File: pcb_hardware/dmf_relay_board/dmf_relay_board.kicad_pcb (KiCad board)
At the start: 4 copper layers, 100 x 96.5 mm, 76 parts, among them J1 HVPS, J2 Relays to Electrodes 1, J3 Relays to Electrodes 2, J4 Electrodes from Relay 1, J5 Electrodes from Relay 2, M1 MountingHole_3.2mm_M3, M2 MountingHole_3.2mm_M3, M3 MountingHole_3.2mm_M3, M4 MountingHole_3.2mm_M3, M5 MountingHole_3.2mm_M3, M6 MountingHole_3.2mm_M3, U1 HV507

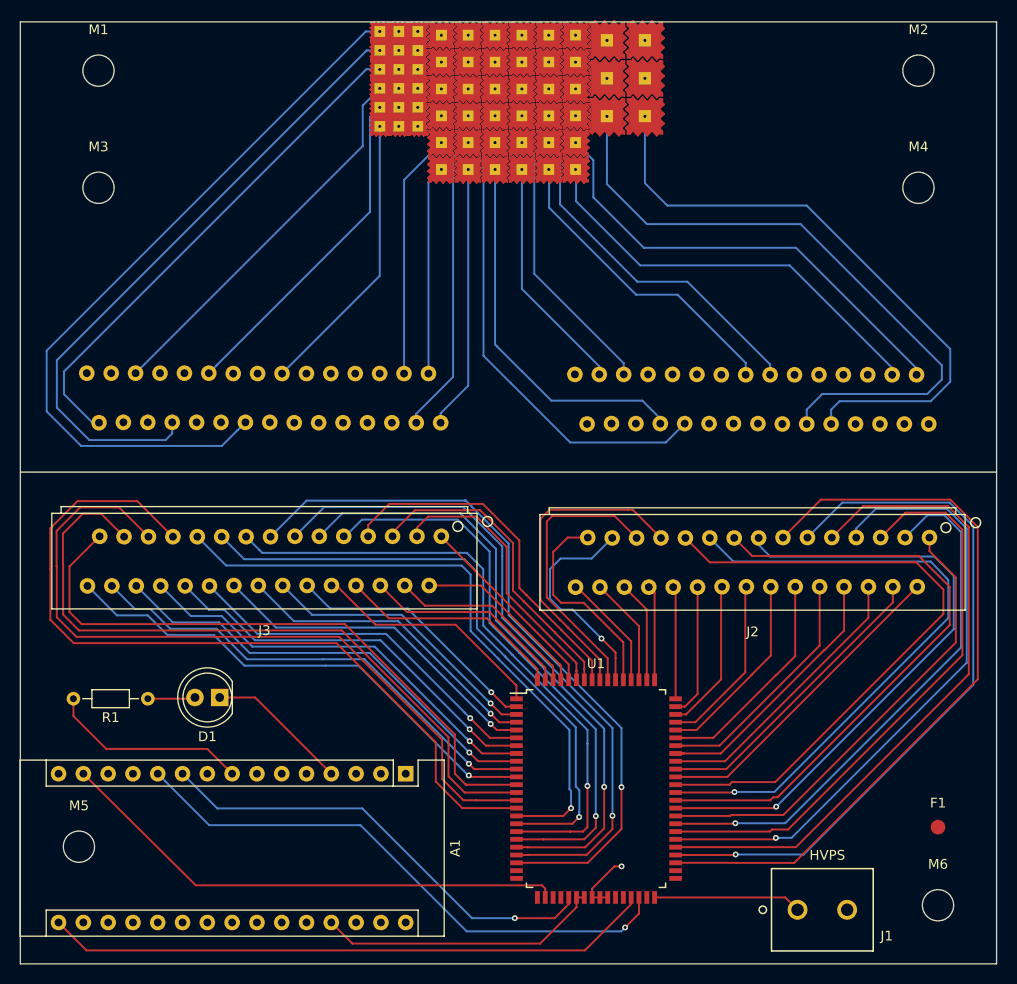
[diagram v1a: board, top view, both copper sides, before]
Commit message: hvps and low voltage isolated
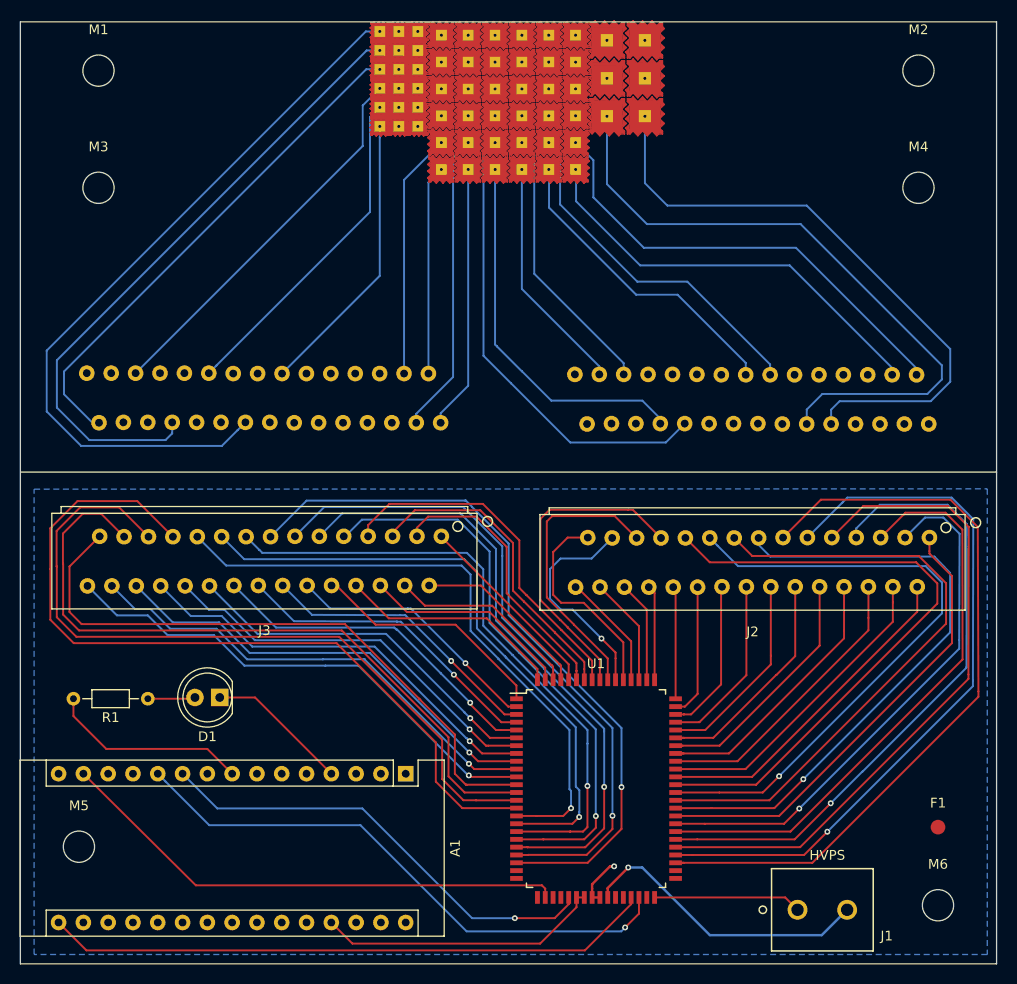
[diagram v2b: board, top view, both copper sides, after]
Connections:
- J1 pad 2: GND -> GNDPWR
- U1 pad 34: GND -> GNDPWR
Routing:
- net GNDPWR: track 0.00 -> 30.3 mm, vias 0 -> 1
- net CHNL_3: track 77.1 -> 79.0 mm
- net CHNL_12: track 65.5 -> 63.7 mm
- net CHNL_14: track 32.8 -> 34.3 mm
- net CHNL_13: track 65.8 -> 64.3 mm
- net GND: track 21.1 -> 19.8 mm
- net CHNL_15: track 30.9 -> 32.1 mm
- net CHNL_4: track 73.5 -> 74.3 mm
- net CHNL_6: track 65.0 -> 65.9 mm
- net CHNL_16: track 29.0 -> 29.8 mm
- net CHNL_11: track 63.6 -> 63.0 mm
- net CHNL_8: track 56.0 -> 55.4 mm
- net CHNL_9: track 47.9 -> 47.4 mm
- net CHNL_20: track 20.0 -> 20.5 mm
- added copper zone on B.Cu, net GND
- removed copper zone on In2.Cu, net GND
- removed copper zone on In1.Cu, net VPP
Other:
- net class DMF_HV: clearance 0.2 -> 0.4

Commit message: hv power isolated
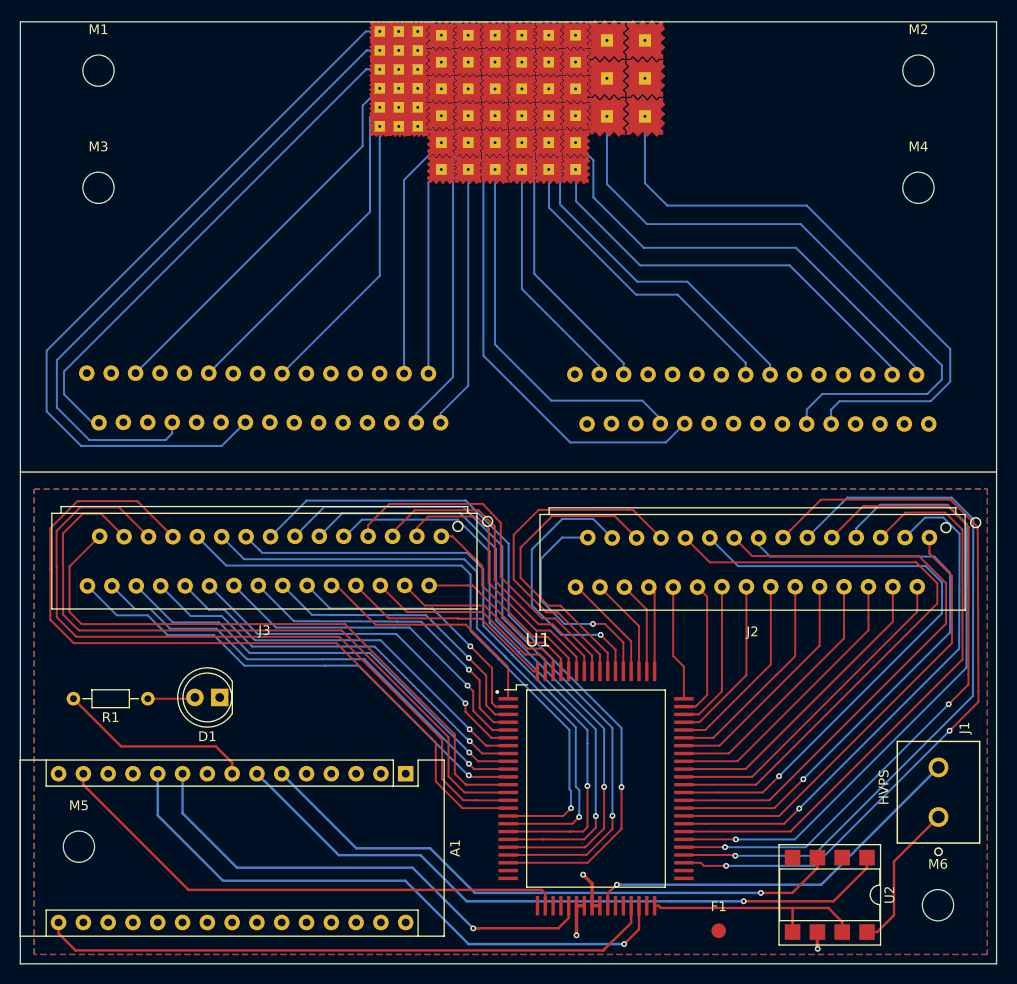
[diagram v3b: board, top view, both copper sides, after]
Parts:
- added U2: AQW210EHAX, Package_DIP:DIP-8_W7.62mm_SMDSocket_SmallPads, F.Cu at (194.9, 143.5)
- U1: footprint Package_QFP:PQFP-80_14x20mm_P0.8mm -> HV507:QFP80P2390X1790X340-80N
- moved F1 24.8 mm to (183.5, 147.2)
- moved J1 17.3 mm to (206.0, 135.5), turned to 90 degrees
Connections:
- A1 pad 6: Net-(A1-Pad6) -> RELAY_VDD
- A1 pad 7: Net-(A1-Pad7) -> RELAY_VPP
- J1 pad 1: VPP -> HVPS_VPP
- U1 pad 40: VPP -> HV507_VPP
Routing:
- net RELAY_VPP: track 0.00 -> 70.4 mm, vias 0 -> 1
- net RELAY_VDD: track 0.00 -> 62.0 mm, vias 0 -> 1
- net HV507_VPP: track 0.00 -> 23.4 mm
- net VDD: track 29.4 -> 6.56 mm, vias 0 -> 2
- net GND: track 19.8 -> 4.37 mm
- net HVPS_VPP: track 0.00 -> 15.4 mm
- net VPP: track 15.2 -> 0.00 mm
- net GNDPWR: track 30.3 -> 40.5 mm
- net CHNL_30: track 22.5 -> 28.7 mm
- net ~LE: track 58.4 -> 63.8 mm
- net CHNL_32: track 32.9 -> 37.2 mm
- net ~BL: track 47.0 -> 50.9 mm
- net CHNL_29: track 21.6 -> 24.0 mm, vias 0 -> 1
- net CHNL_44: track 32.2 -> 34.6 mm
- net CHNL_36: track 20.1 -> 22.4 mm
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- added copper zone on F.Cu, net GND
- added copper zone on B.Cu, net VDD
- removed copper zone on B.Cu, net GND

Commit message: minor changes
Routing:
- net GND: track 4.37 -> 3.81 mm
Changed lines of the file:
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@@
   (gr_line (start 111.9735 54.0412) (end 111.9735 150.536) (layer Edge.Cuts) (width 0.05))
   (gr_line (start 111.9735 150.536) (end 211.9735 150.536) (layer Edge.Cuts) (width 0.05))
-  (via (at 169.6212 141.4018) (size 0.6) (drill 0.3) (layers F.Cu B.Cu) (net 7))
-  (segment (start 170.542 142.3226) (end 169.6212 141.4018) (width 0.35) (layer F.Cu) (net 7))
-  (segment (start 170.542 142.3226) (end 170.542 144.588) (width 0.35) (layer F.Cu) (net 7))
+  (via (at 169.70756 141.92504) (size 0.6) (drill 0.3) (layers F.Cu B.Cu) (net 7))
   (segment (start 170.542 144.588) (end 171.342 144.588) (width 0.35) (layer F.Cu) (net 7))
+  (segment (start 170.542 142.75948) (end 170.542 144.588) (width 0.35) (layer F.Cu) (net 7))
+  (segment (start 169.70756 141.92504) (end 170.542 142.75948) (width 0.35) (layer F.Cu) (net 7))
   (segment (start 133.6675 129.93263) (end 131.99979 128.26492) (width 0.25) (layer F.Cu) (net 13))
   (segment (start 133.6675 131.064) (end 133.6675 129.93263) (width 0.25) (layer F.Cu) (net 13))
@@
   (segment (start 179.942 140.188) (end 179.95184 140.19784) (width 0.2) (layer F.Cu) (net 67))
   (segment (start 179.092 140.188) (end 179.942 140.188) (width 0.2) (layer F.Cu) (net 67))
-  (via (at 207.1624 126.65964) (size 0.6) (drill 0.3) (layers F.Cu B.Cu) (net 67))
-  (segment (start 193.97608 102.99192) (end 190.0975 106.8705) (width 0.2) (layer F.Cu) (net 67))
-  (segment (start 210.04784 105.79354) (end 207.24622 102.99192) (width 0.2) (layer F.Cu) (net 67))
-  (segment (start 207.462399 126.359641) (end 207.467479 126.359641) (width 0.2) (layer F.Cu) (net 67))
-  (segment (start 207.1624 126.65964) (end 207.462399 126.359641) (width 0.2) (layer F.Cu) (net 67))
-  (segment (start 207.467479 126.359641) (end 210.11388 123.71324) (width 0.2) (layer F.Cu) (net 67))
-  (segment (start 207.24622 102.99192) (end 193.97608 102.99192) (width 0.2) (layer F.Cu) (net 67))
-  (segment (start 210.11388 123.71324) (end 210.11388 122.6312) (width 0.2) (layer F.Cu) (net 67))
-  (segment (start 210.11388 122.6312) (end 210.04784 105.79354) (width 0.2) (layer F.Cu) (net 67))
   (segment (start 179.942 140.188) (end 181.68144 140.188) (width 0.2) (layer F.Cu) (net 67))
   (via (at 184.277 140.49756) (size 0.6) (drill 0.3) (layers F.Cu B.Cu) (net 67))
@@
   (segment (start 184.277 140.49756) (end 193.32448 140.49756) (width 0.2) (layer B.Cu) (net 67))
   (segment (start 193.32448 140.49756) (end 193.6496 140.17244) (width 0.2) (layer B.Cu) (net 67))
+  (via (at 209.2706 124.5362) (size 0.6) (drill 0.3) (layers F.Cu B.Cu) (net 67))
+  (segment (start 207.1624 126.65964) (end 207.1624 126.6444) (width 0.2) (layer B.Cu) (net 67))
+  (segment (start 207.1624 126.6444) (end 209.2706 124.5362) (width 0.2) (layer B.Cu) (net 67))
+  (segment (start 193.97608 102.99192) (end 190.0975 106.8705) (width 0.2) (layer F.Cu) (net 67))
+  (segment (start 210.11388 123.69292) (end 210.11388 122.6312) (width 0.2) (layer F.Cu) (net 67))
+  (segment (start 209.2706 124.5362) (end 210.11388 123.69292) (width 0.2) (layer F.Cu) (net 67))
+  (segment (start 210.11388 122.6312) (end 210.04784 105.79354) (width 0.2) (layer F.Cu) (net 67))
+  (segment (start 210.04784 105.79354) (end 207.24622 102.99192) (width 0.2) (layer F.Cu) (net 67))
+  (segment (start 207.24622 102.99192) (end 193.97608 102.99192) (width 0.2) (layer F.Cu) (net 67))
   (segment (start 179.092 139.388) (end 180.82556 139.388) (width 0.2) (layer F.Cu) (net 68))
   (segment (start 179.942 139.388) (end 185.12324 139.388) (width 0.2) (layer F.Cu) (net 68))

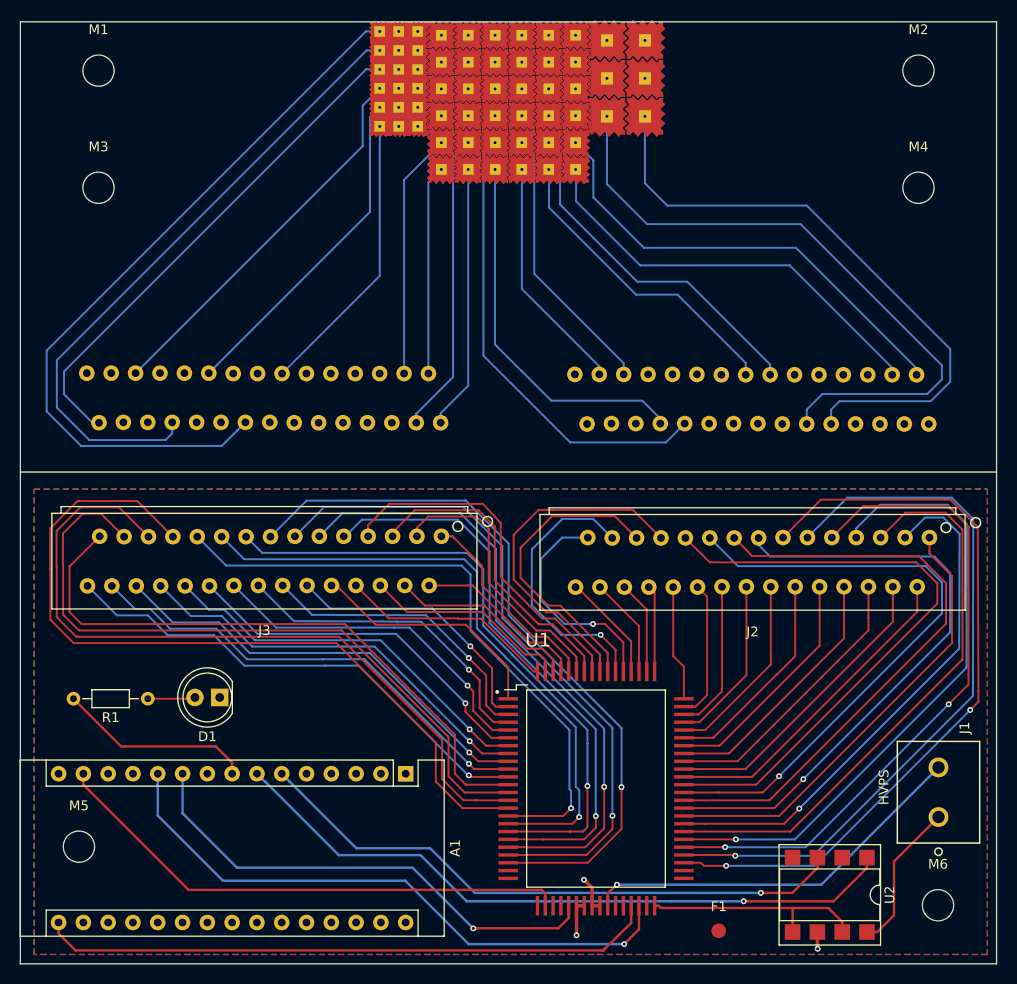
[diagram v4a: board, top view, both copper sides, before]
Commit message: pull-resistors for relays
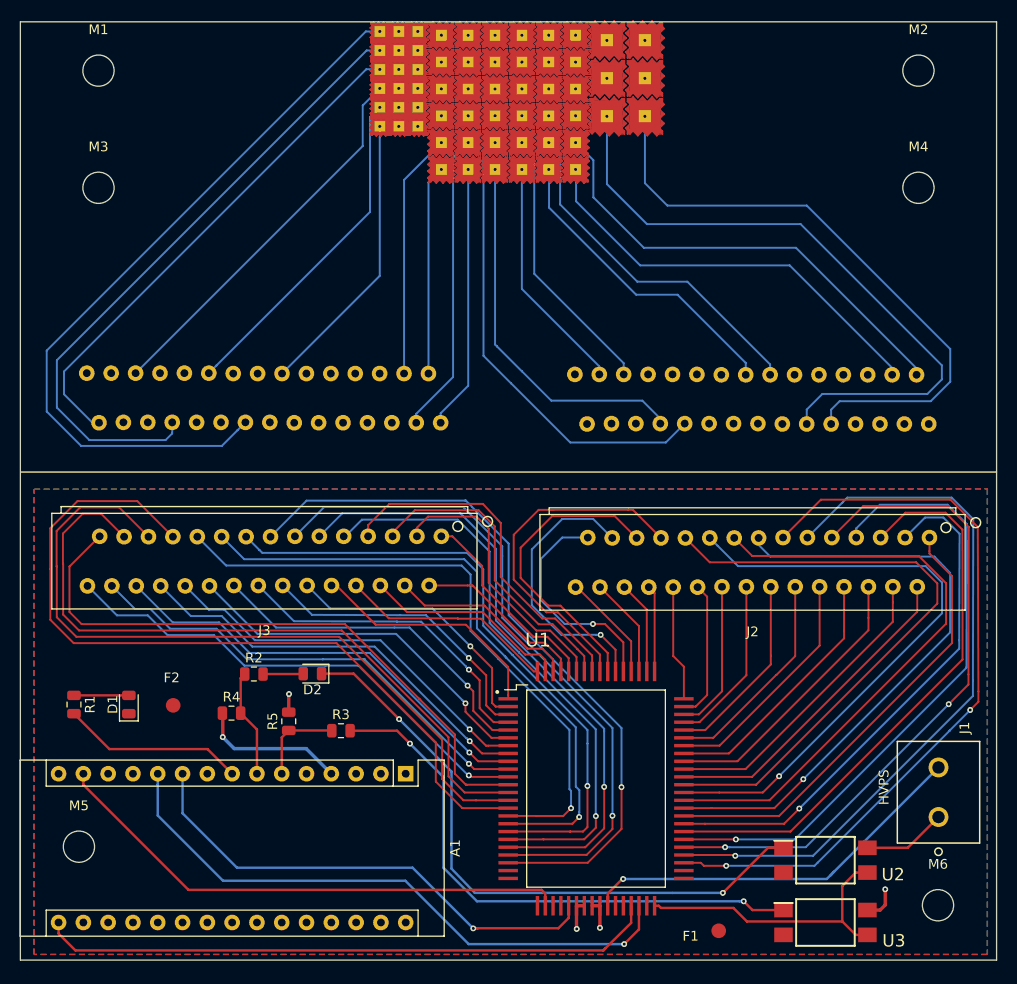
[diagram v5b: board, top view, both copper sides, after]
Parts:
- added D2: GREEN LED, LED_SMD:LED_0805_2012Metric, F.Cu at (141.9, 120.8)
- added F2: Fiducial_1.5mm_Mask3mm, Fiducial:Fiducial_1.5mm_Mask3mm, F.Cu at (127.6, 124.1)
- added R2: 750, Resistor_SMD:R_0805_2012Metric, F.Cu at (135.9, 120.9)
- added R3: 560, Resistor_SMD:R_0805_2012Metric, F.Cu at (144.8, 126.7)
- added R4: 10k, Resistor_SMD:R_0805_2012Metric, F.Cu at (133.6, 124.9)
- added R5: 330, Resistor_SMD:R_0805_2012Metric, F.Cu at (139.5, 125.7)
- added U3: AQY210EHA, SamacSys_Parts:SOP254P962X315-4N, F.Cu at (194.4, 146.3)
- D1: value LED -> BLUE LED; footprint LED_THT:LED_D5.0mm_FlatTop -> LED_SMD:LED_0805_2012Metric
- R1: value R -> 1k; footprint Resistor_THT:R_Axial_DIN0204_L3.6mm_D1.6mm_P7.62mm_Horizontal -> Resistor_SMD:R_0805_2012Metric
- U2: value AQW210EHAX -> AQY210EHA; footprint Package_DIP:DIP-8_W7.62mm_SMDSocket_SmallPads -> SamacSys_Parts:SOP254P962X315-4N
- moved D1 9.34 mm to (123.1, 124.0), turned to 90 degrees
- moved R1 7.59 mm to (117.5, 124.0), turned to 270 degrees
- moved U2 3.58 mm to (194.4, 139.9), turned to 0 degrees
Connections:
- A1 pad 6: RELAY_VDD -> Net-(A1-Pad6)
- A1 pad 7: RELAY_VPP -> Net-(A1-Pad7)
- U2 pad 1: RELAY_VPP -> VPP_ON
- U2 pad 3: RELAY_VDD -> HV507_VPP
- U2 pad 4: GND -> HVPS_VPP
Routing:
- net RELAY_VPP: track 70.4 -> 0.00 mm, vias 1 -> 0
- net VPP_ON: track 0.00 -> 64.4 mm, vias 0 -> 2
- net RELAY_VDD: track 62.0 -> 0.00 mm, vias 1 -> 0
- net VDD_ON: track 0.00 -> 57.4 mm, vias 0 -> 2
- net GND: track 3.81 -> 18.2 mm, vias 1 -> 2
- net Net-(A1-Pad7): track 0.00 -> 11.1 mm
- net Net-(A1-Pad6): track 0.00 -> 9.15 mm
- net HVPS_VPP: track 15.4 -> 8.59 mm
- net HV507_VPP: track 23.4 -> 29.8 mm
- net Net-(D2-Pad2): track 0.00 -> 4.76 mm
- net VDD: track 6.56 -> 9.70 mm, vias 2 -> 3
- net Net-(A1-Pad8): track 20.1 -> 18.8 mm
- net Net-(D1-Pad2): track 4.88 -> 5.62 mm
- net GNDPWR: track 40.5 -> 41.0 mm
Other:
- board size 100 x 96.5 mm -> 100 x 96.1 mm

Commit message: hv data direction fix
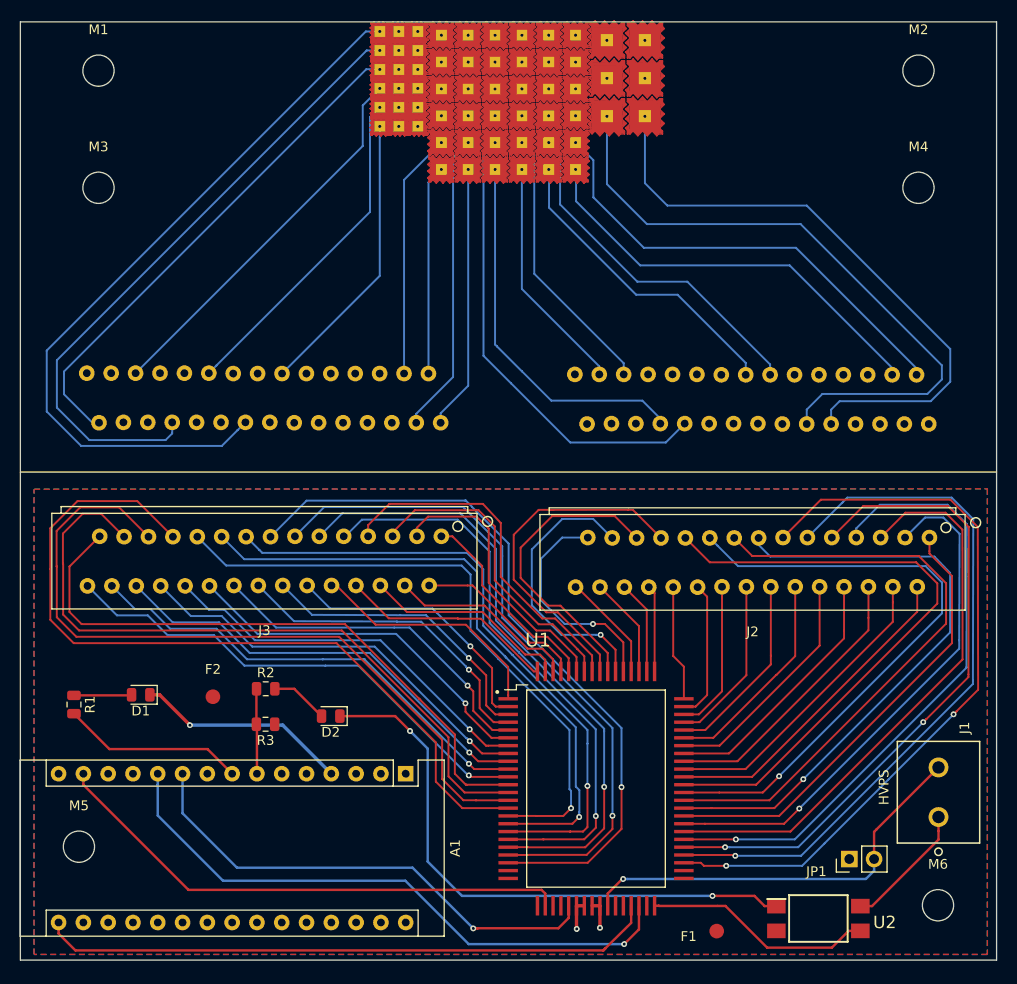
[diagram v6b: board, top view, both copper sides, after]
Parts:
- removed R4: 10k, Resistor_SMD:R_0805_2012Metric
- removed R5: 330, Resistor_SMD:R_0805_2012Metric
- removed U3: AQY210EHA, SamacSys_Parts:SOP254P962X315-4N
- added JP1: GND to HV-GND Jumper, Connector_PinHeader_2.54mm:PinHeader_1x02_P2.54mm_Vertical, F.Cu at (196.9, 139.8)
- R3: value 560 -> 10k
- moved R3 7.75 mm to (137.1, 126.0), turned to 180 degrees
- moved U2 6.02 mm to (193.7, 145.9)
- moved D2 4.74 mm to (143.8, 125.2)
- moved F2 4.17 mm to (131.7, 123.2)
- moved R2 1.94 mm to (137.1, 122.4)
- moved D1 1.57 mm to (124.3, 123.0), turned to 180 degrees
- moved F1 0.21 mm to (183.3, 147.2)
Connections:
- R3 pad 1: Net-(A1-Pad6) -> GND
- R3 pad 2: VDD_ON -> Net-(A1-Pad7)
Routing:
- net VDD_ON: track 57.4 -> 0.00 mm, vias 2 -> 0
- net Net-(A1-Pad6): track 9.15 -> 0.00 mm
- net GND: track 18.2 -> 25.0 mm
- net HV507_VPP: track 29.8 -> 23.6 mm
- net VDD: track 9.70 -> 4.19 mm, vias 3 -> 1
- net VPP_ON: track 64.4 -> 59.6 mm
- net HVPS_VPP: track 8.59 -> 13.1 mm
- net Net-(A1-Pad7): track 11.1 -> 8.78 mm
- net GNDPWR: track 41.0 -> 42.8 mm
- net Net-(D2-Pad2): track 4.76 -> 5.94 mm
- net CHNL_3: track 78.8 -> 78.0 mm
- net CHNL_4: track 75.9 -> 75.1 mm
